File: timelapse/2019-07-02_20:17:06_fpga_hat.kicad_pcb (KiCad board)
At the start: 4 copper layers, 65 x 56.5 mm, 90 parts, among them J1 2x20, J2 AudioJack3, J3 Conn_02x06_Top_Bottom, J4 Conn_02x06_Top_Bottom, J5 Conn_02x06_Top_Bottom, J6 Conn_01x02, SW1 PTS815, SW2 PTS815, SW3 PTS815, SW4 PTS815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

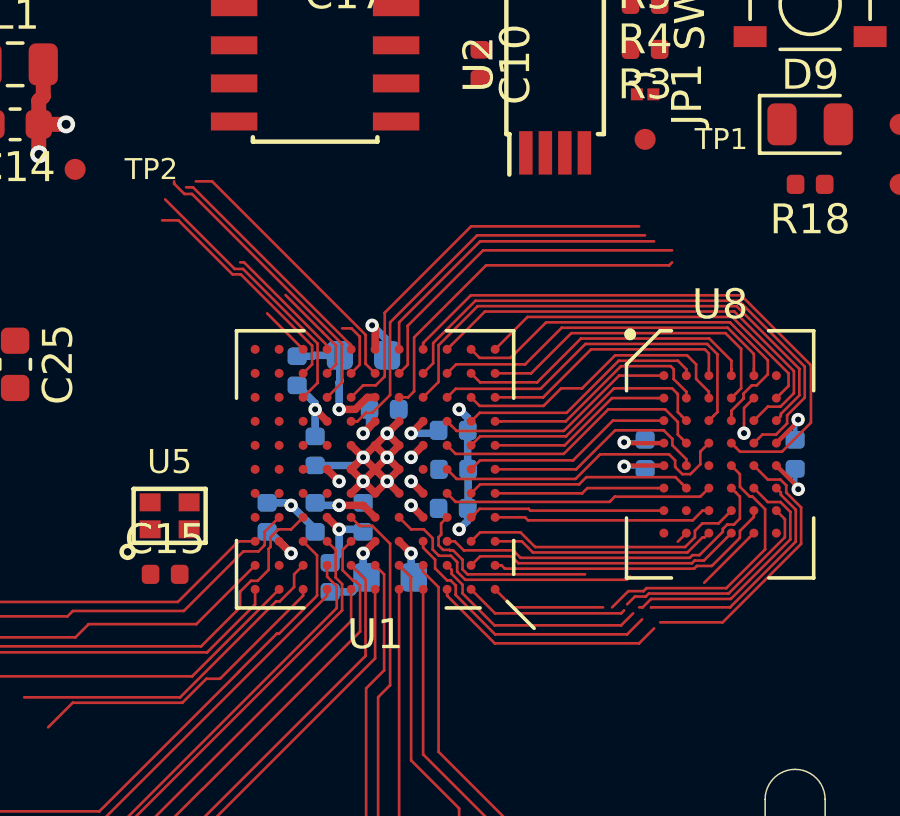
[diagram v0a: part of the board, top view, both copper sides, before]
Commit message: SRAM escaped. Some work on FPGA power routing. Some SRAM pinswapping.
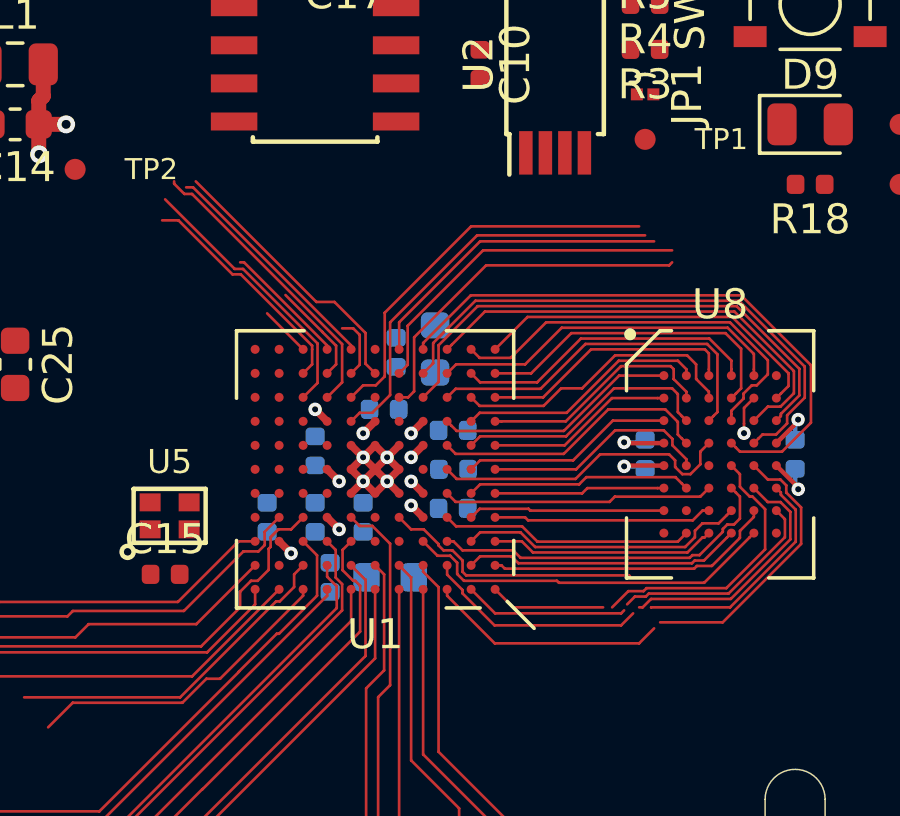
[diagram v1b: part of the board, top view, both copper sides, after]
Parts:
- moved R2 3.36 mm to (133.2, 102.6), turned to 90 degrees
- moved C2 2.40 mm to (134.5, 102.5), turned to 90 degrees
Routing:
- net GND: track 24.9 -> 14.2 mm, vias 11 -> 7
- net +1V2: track 12.7 -> 7.71 mm
- net Net-(C2-Pad1): track 4.61 -> 0.00 mm, vias 1 -> 0
- net +3V3: track 10.9 -> 6.70 mm, vias 8 -> 7
- net Net-(C4-Pad1): track 2.83 -> 0.00 mm, vias 1 -> 0
- net Net-(C2-Pad2): track 2.05 -> 0.00 mm, vias 1 -> 0
- net /SRAM_A8: track 6.93 -> 8.43 mm
- net Net-(C4-Pad2): track 1.40 -> 0.00 mm, vias 1 -> 0
- net /SRAM_A11: track 11.6 -> 12.5 mm
